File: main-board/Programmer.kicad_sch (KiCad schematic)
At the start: 68 parts, among them U1 FT4232HL, U14 TS5A23159DGS, U17 74AHC244, U28 TS5A23159DGS, U31 74AHC244, U9 74AHCT1G08, Y1 Crystal_GND24

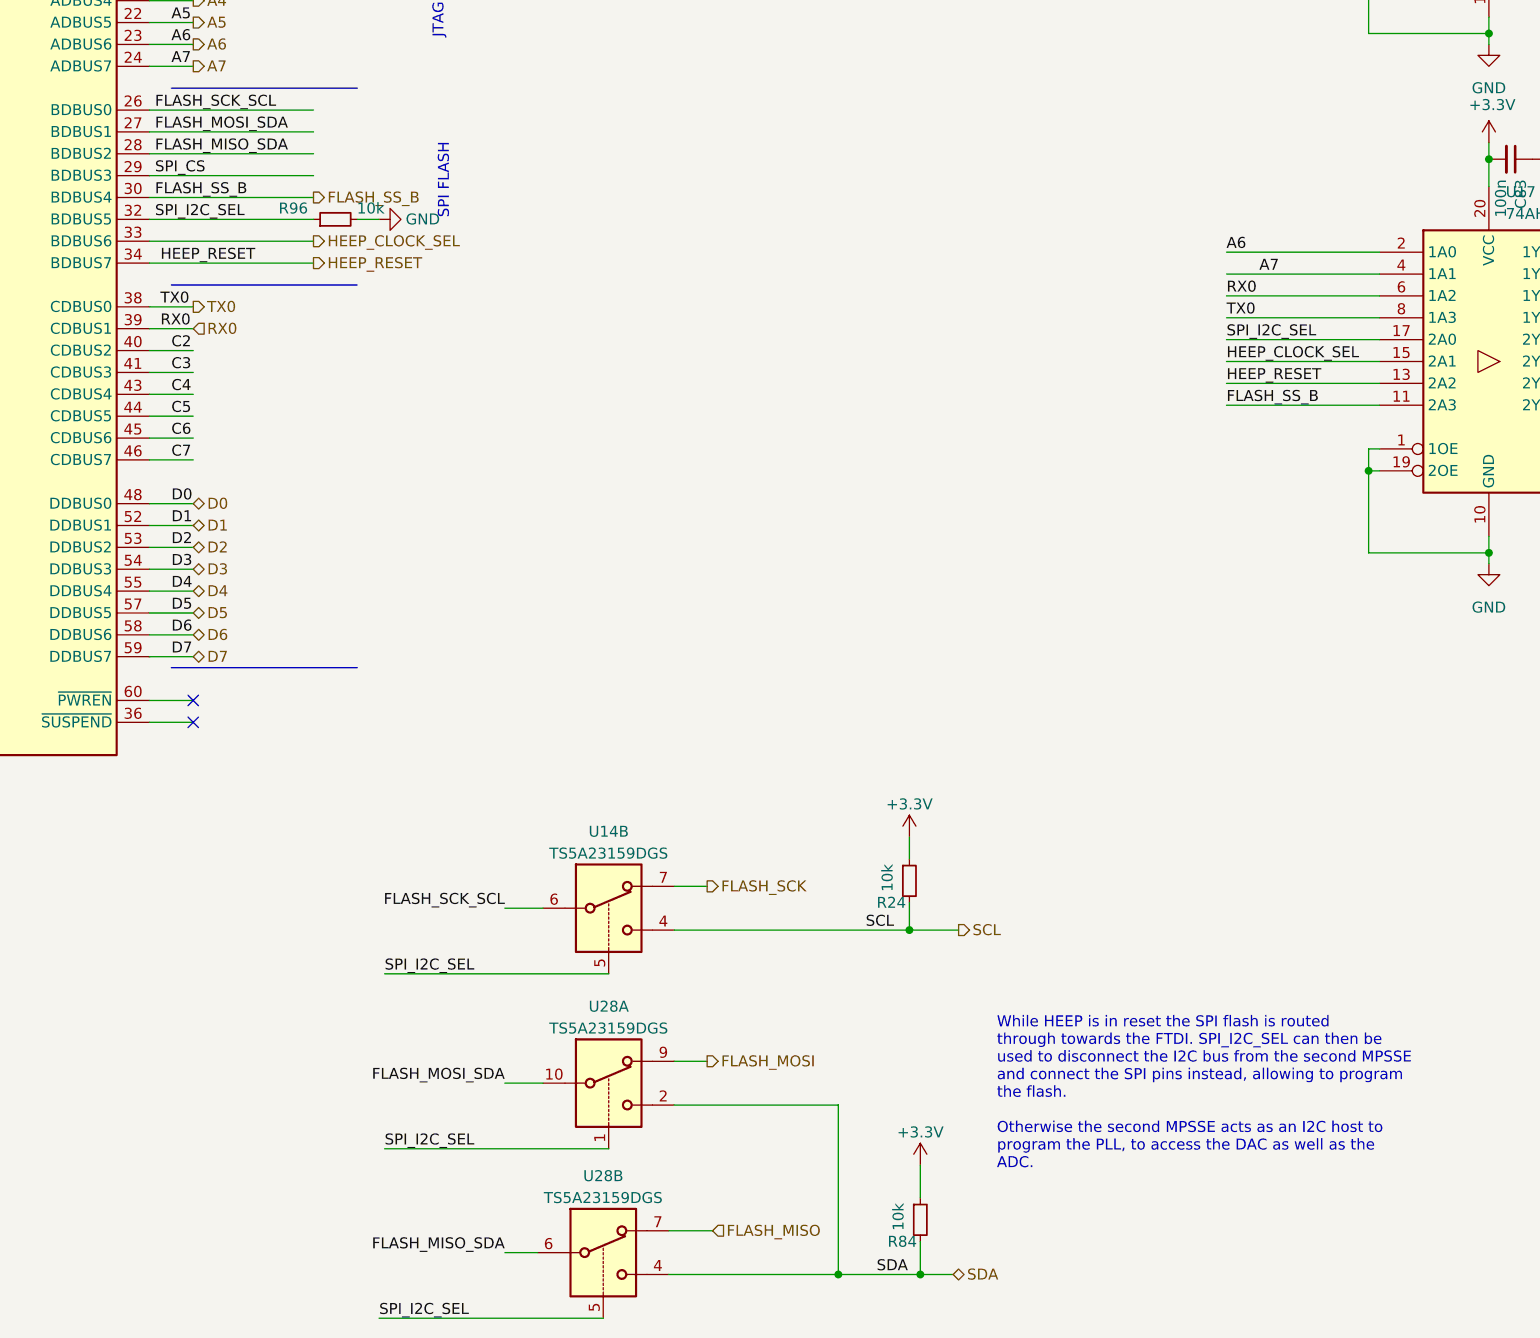
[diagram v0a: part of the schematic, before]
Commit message: re-arranged adc/dac and routed to the cgs
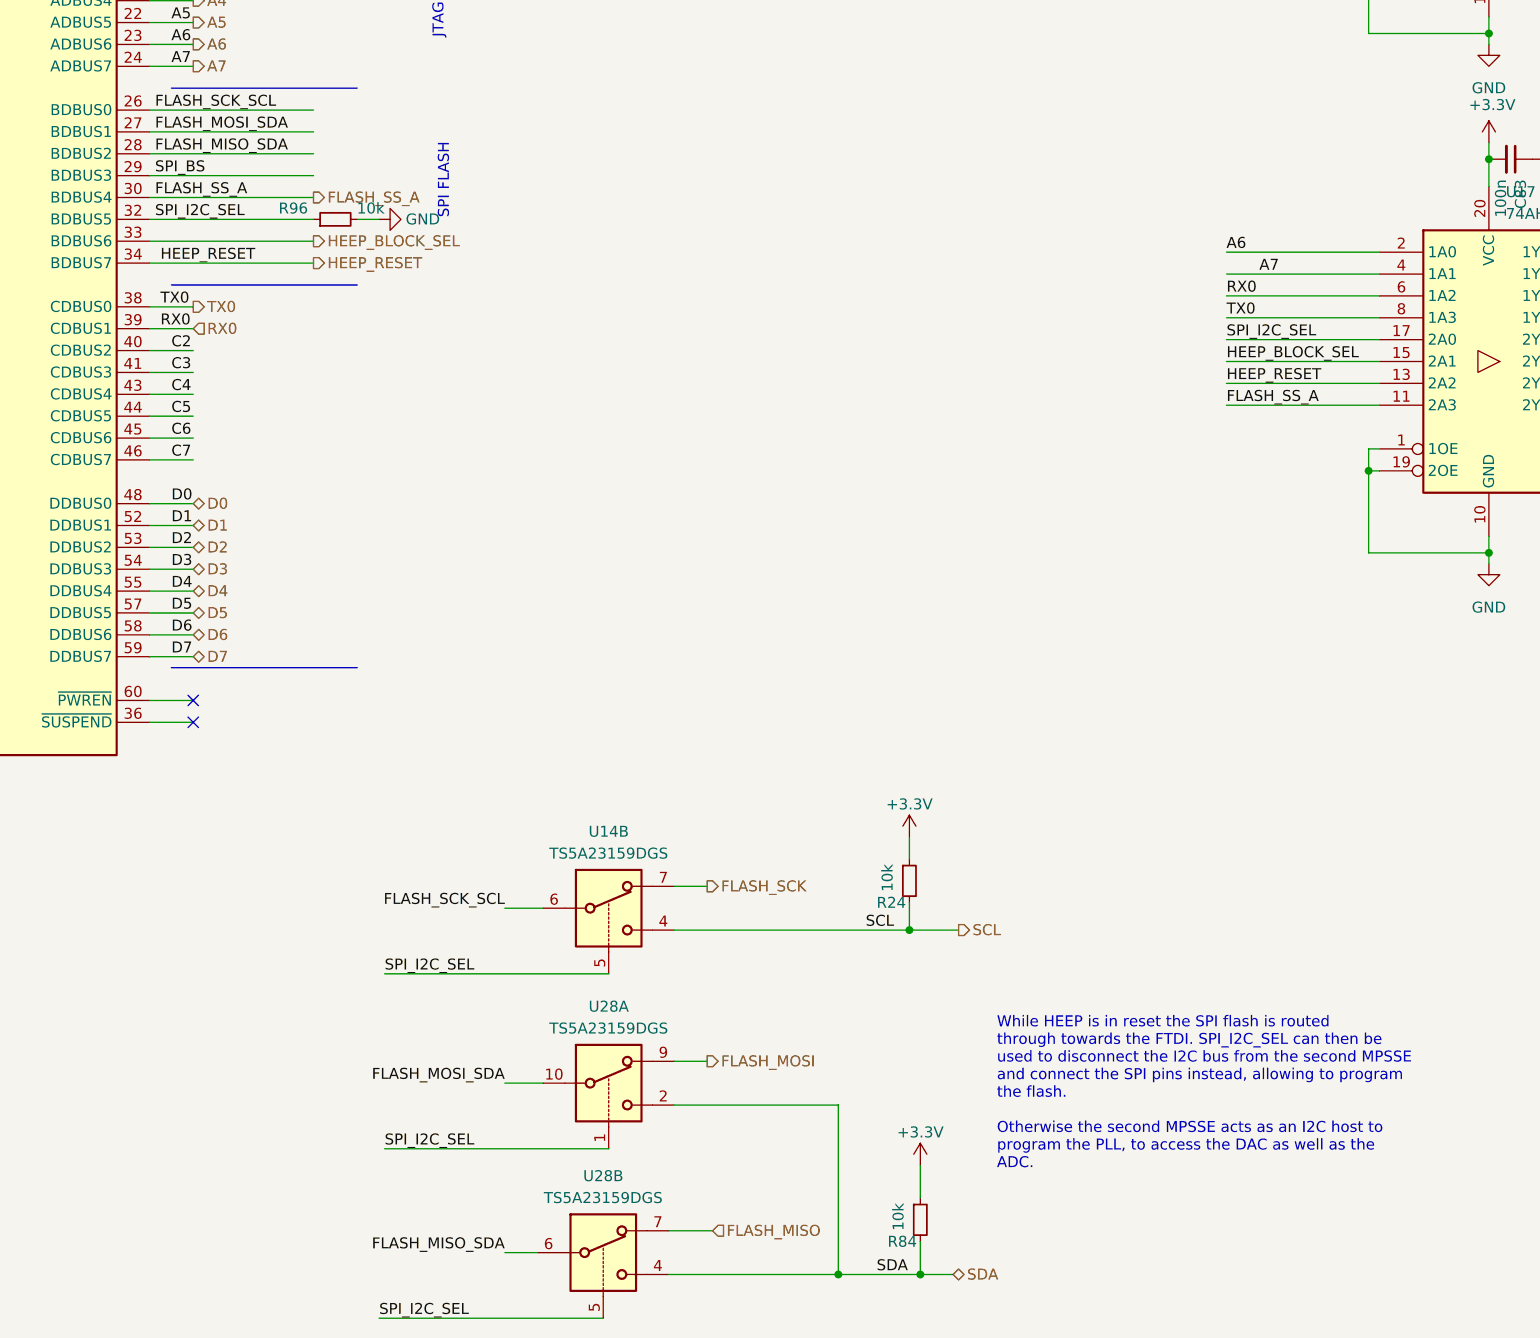
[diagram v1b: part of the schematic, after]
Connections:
- net FLASH_SS_B renamed FLASH_SS_A
- net HEEP_CLOCK_SEL renamed HEEP_BLOCK_SEL
- net SPI_CS renamed SPI_BS

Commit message: Before re-organizing the main board
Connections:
- net +3.3V renamed 3V3
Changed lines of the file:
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@@
 			)
 		)
-		(property "Value" "+3.3V"
+		(property "Value" "3V3"
 			(at 317.881 21.6408 0)
 			(effects
@@
 			)
 		)
-		(property "Value" "+3.3V"
+		(property "Value" "3V3"
 			(at 95.631 57.2008 0)
 			(effects
@@
 			)
 		)
-		(property "Value" "+3.3V"
+		(property "Value" "3V3"
 			(at 251.46 205.105 0)
 			(effects
@@
 			)
 		)
-		(property "Value" "+3.3V"
+		(property "Value" "3V3"
 			(at 120.396 26.0858 0)
 			(effects
@@
 			)
 		)
-		(property "Value" "+3.3V"
+		(property "Value" "3V3"
 			(at 317.881 85.7758 0)
 			(effects
@@
 			)
 		)
-		(property "Value" "+3.3V"
+		(property "Value" "3V3"
 			(at 148.336 43.8658 0)
 			(effects
@@
 			)
 		)
-		(property "Value" "+3.3V"
+		(property "Value" "3V3"
 			(at 52.451 85.1408 0)
 			(effects
@@
 			)
 		)
-		(property "Value" "+3.3V"
+		(property "Value" "3V3"
 			(at 250.19 167.005 0)
 			(effects

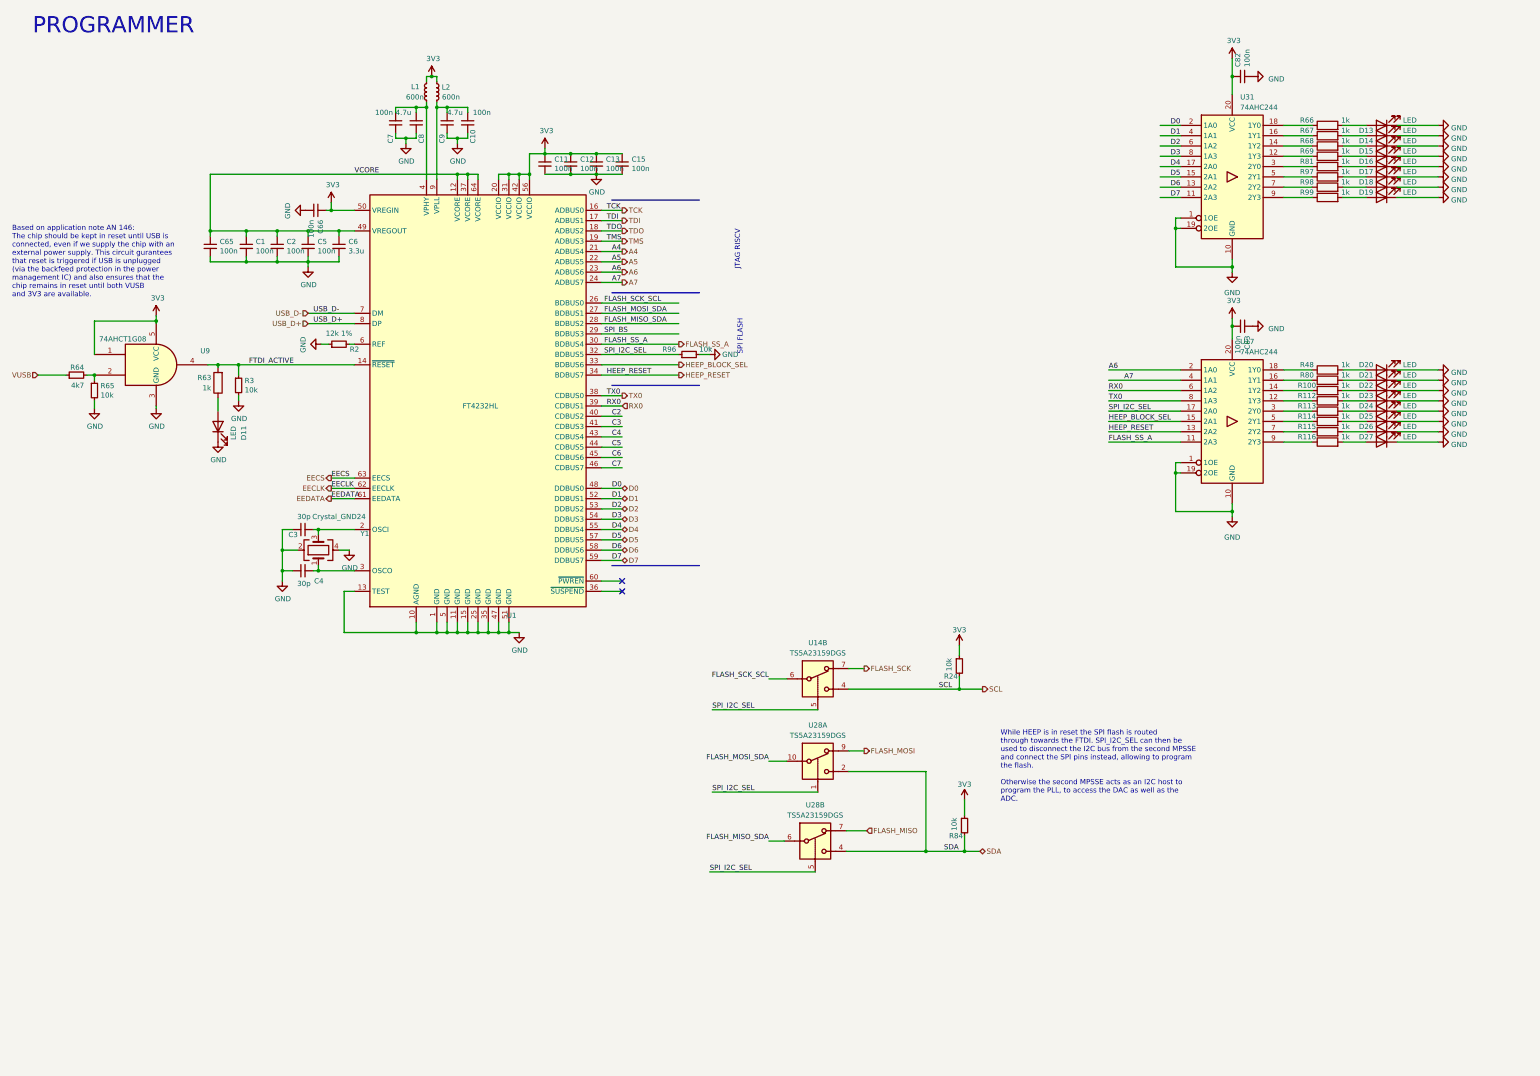
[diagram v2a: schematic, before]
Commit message: Before re-routing programmer
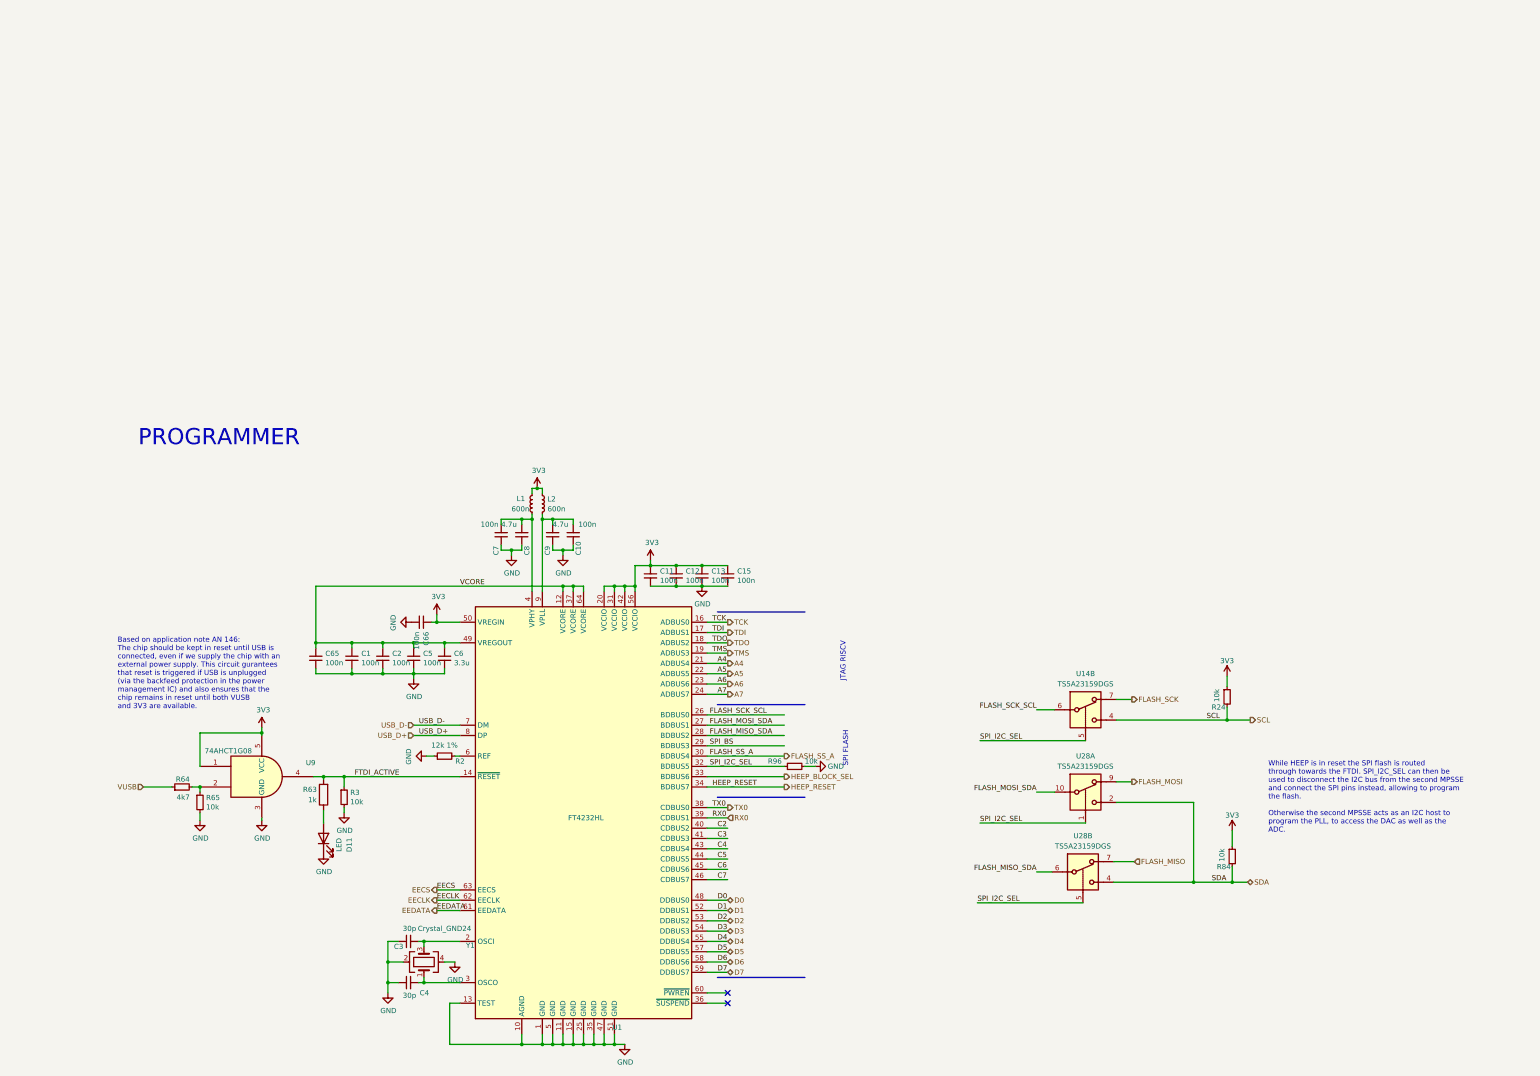
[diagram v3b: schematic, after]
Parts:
- removed C82, C83: 100n, Capacitor_SMD:C_0603_1608Metric, symbol Device:C_Small
- removed D12, D13, D14, D15, D16, D17, D18, D19, D20, D21, D22, D23, D24, D25, D26, D27: LED, LED_SMD:LED_0603_1608Metric, symbol Device:LED
- removed R100, R112, R113, R114, R115, R116, R48, R66, R67, R68, R69, R80, R81, R97, R98, R99: 1k, Resistor_SMD:R_0603_1608Metric, symbol Device:R
- removed U17, U31: 74AHC244, Package_SO:TSSOP-20_4.4x6.5mm_P0.65mm, symbol 74xx:74AHC244
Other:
- moved on the sheet: C1, C10, C11, C12, C13, C15, C2, C3, C4, C5, C6, C65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
